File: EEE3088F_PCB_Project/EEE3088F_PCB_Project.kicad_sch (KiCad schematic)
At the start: 31 parts, among them IC1 DRV8833PWPR, IC2 DRV8833PWPR, IC3 TPS62067DSGR, IC4 TPS62067DSGR, IC5 INA219AIDCNR, J1 Conn_02x16_Odd_Even, Q3 MMBT2222A, Q4 MMBT2222A, Q5 AO3401A, Q6 AO3401A

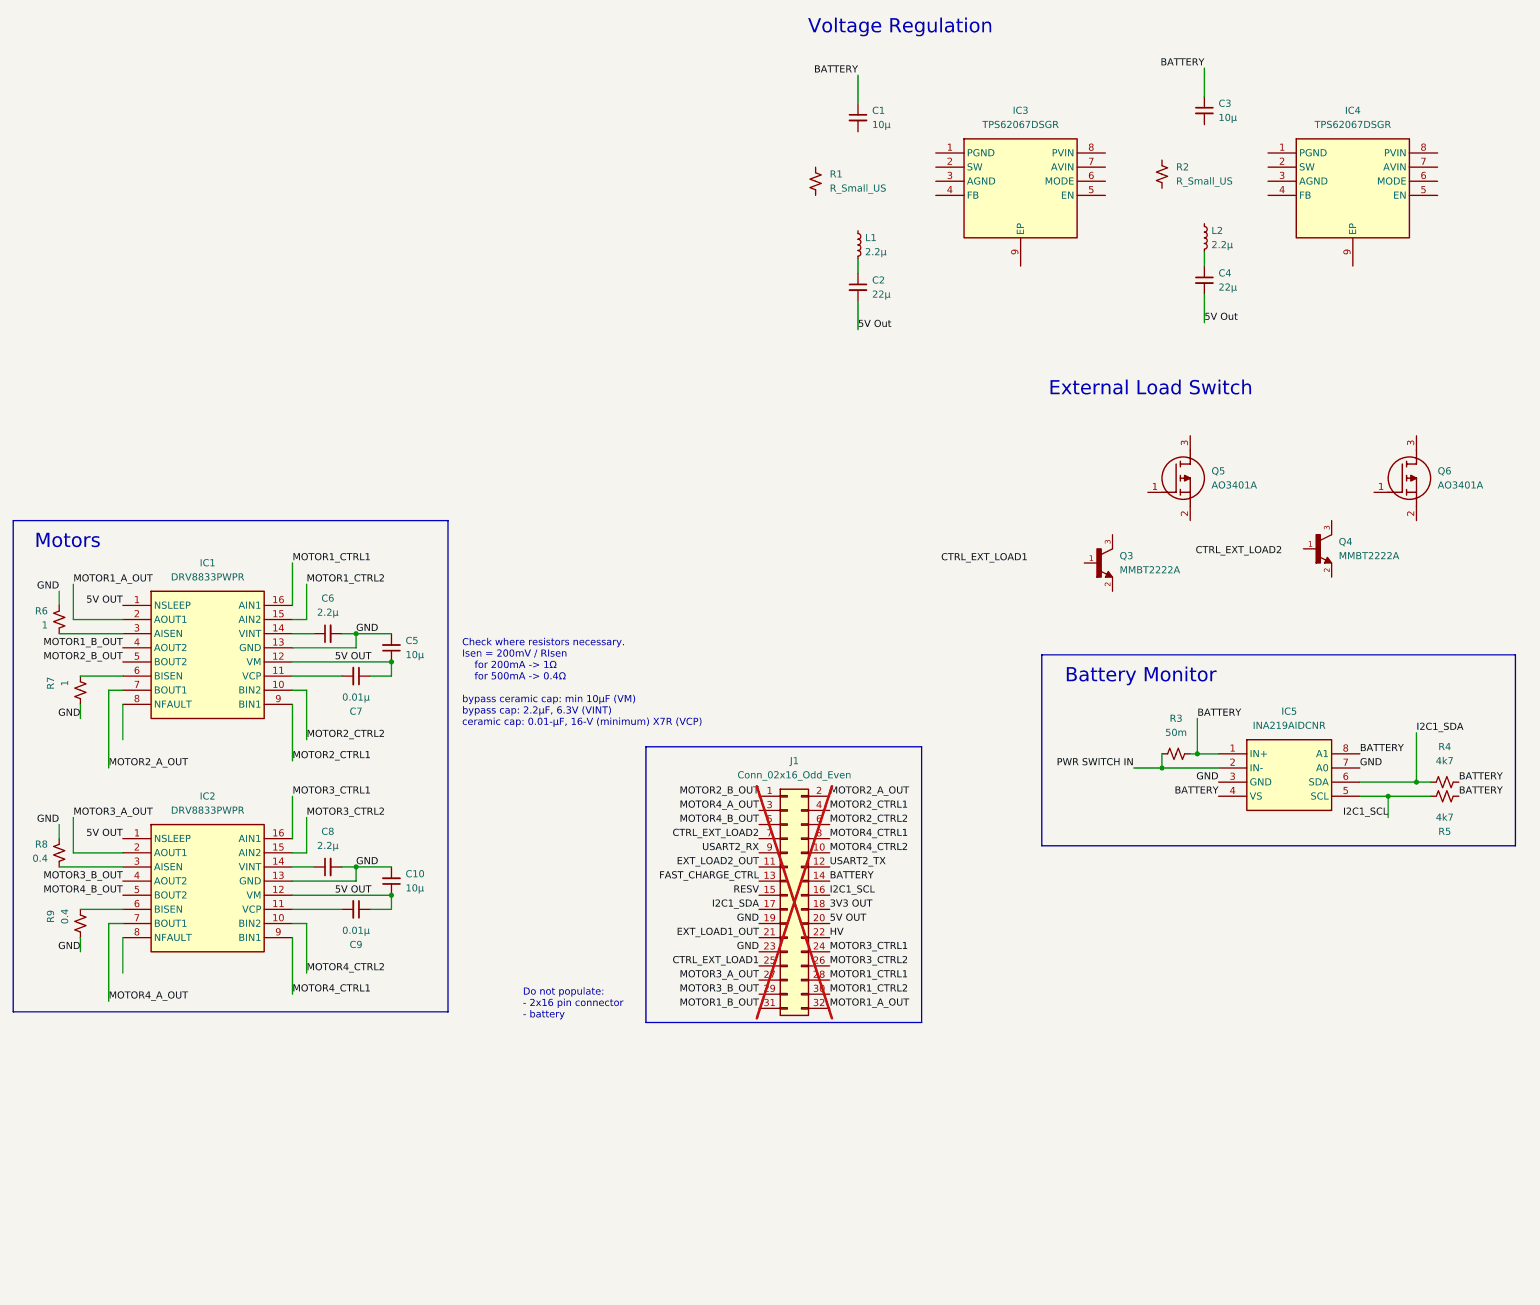
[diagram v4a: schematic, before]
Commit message: v0.4
Lula: rough voltage regulator circuits done but bias resistor values not calculated
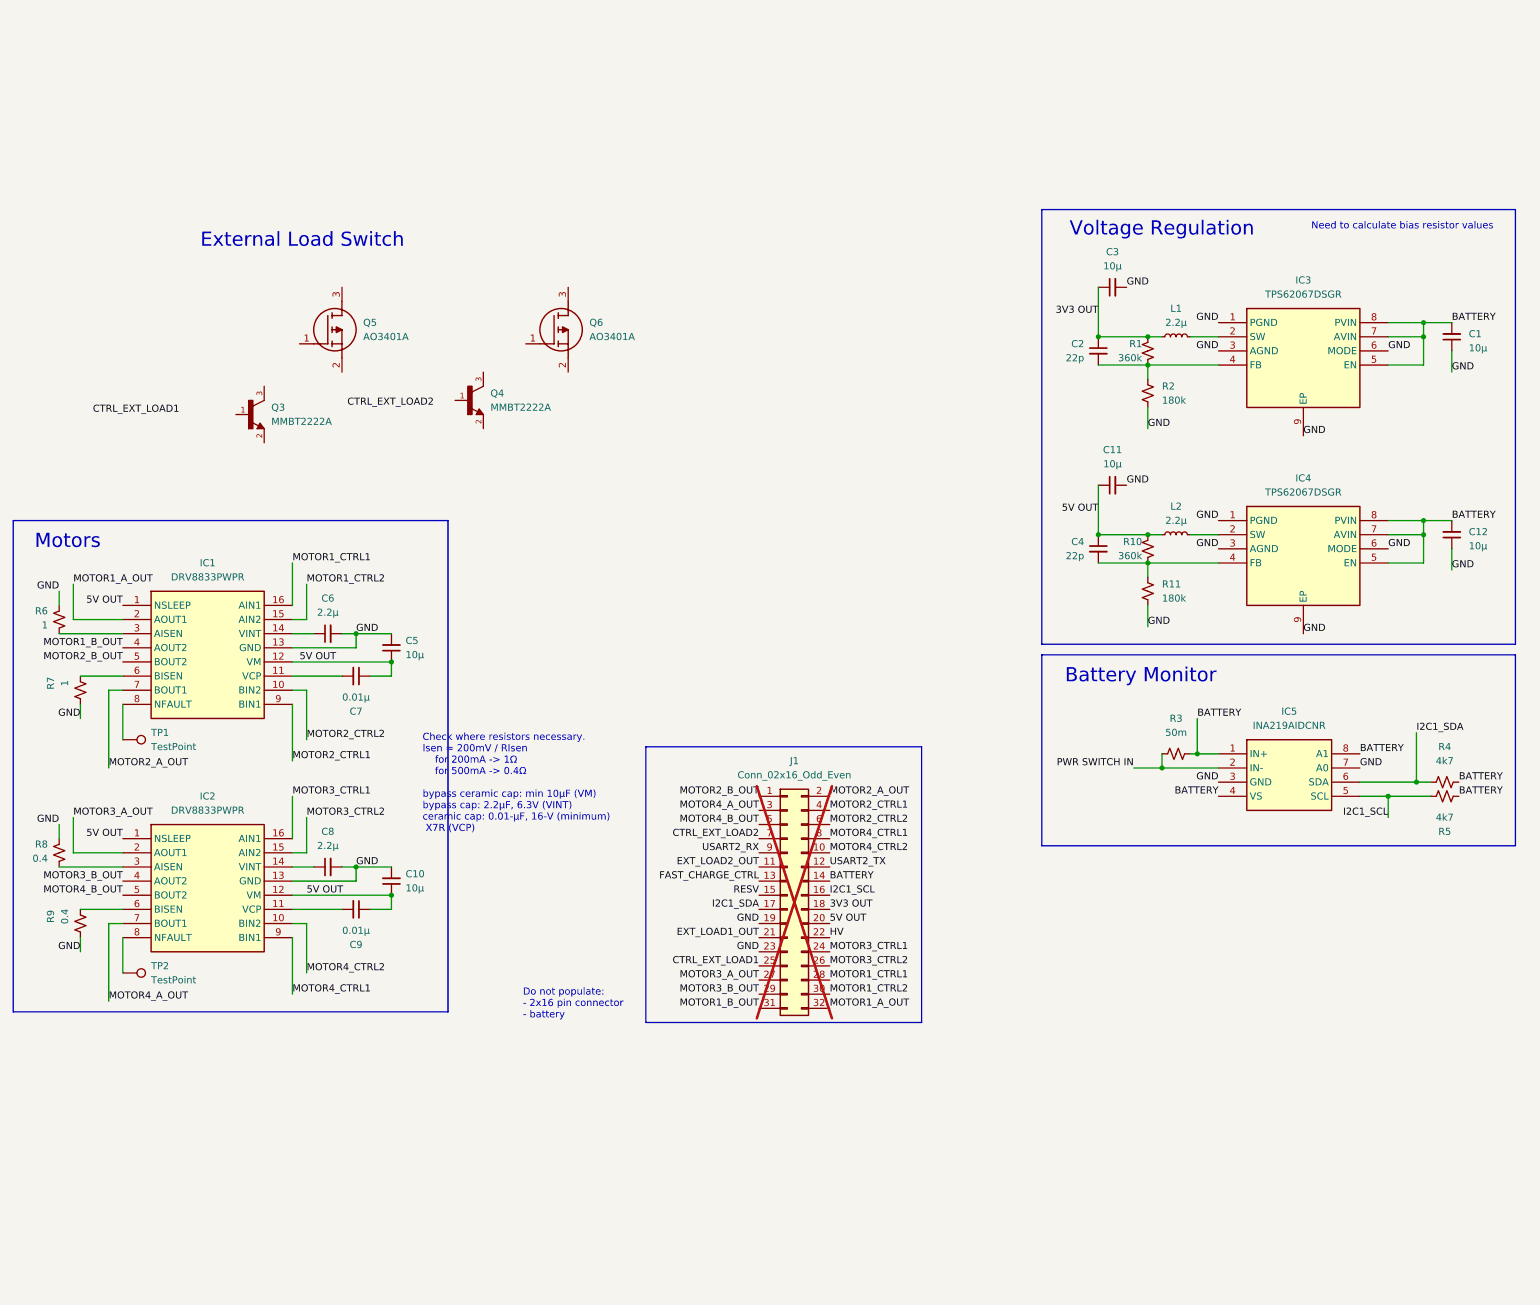
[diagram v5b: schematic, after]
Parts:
- added C11, C12: 10µ, symbol Device:C_Small
- added R10: 360k, symbol Device:R_Small_US
- added R11: 180k, symbol Device:R_Small_US
- added TP1, TP2: TestPoint, symbol Connector:TestPoint
- C2, C4: value 22µ -> 22p
- R1: value R_Small_US -> 360k
- R2: value R_Small_US -> 180k
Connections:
- net 3V3 OUT: now also C2.1, C3.1, L1.1, R1.1
- net 5V OUT: now also C4.1, L2.1, C11.1, R10.1
- net BATTERY: now also C1.2, IC3.5 (EN), IC3.7 (AVIN), IC3.8 (PVIN), IC4.5 (EN), IC4.7 (AVIN), IC4.8 (PVIN), C12.2; no longer C1.1, C3.1
- net GND: now also C1.1, C3.2, IC3.1 (PGND), IC3.3 (AGND), IC3.6 (MODE), IC3.9 (EP), IC4.1 (PGND), IC4.3 (AGND), IC4.6 (MODE), IC4.9 (EP), R2.2, C11.2, C12.1, R11.2
- net at IC3.2 (SW): now also L1.2
- net at IC3.4 (FB): now also C2.2, R1.2, R2.1
- net at IC2.8 (NFAULT): now also TP2.1
- net at L2.2: now also IC4.2 (SW); no longer C4.1
- net at IC1.8 (NFAULT): now also TP1.1
- net at IC4.4 (FB): now also C4.2, R10.2, R11.1
- removed net 5V Out: C2.2, C4.2
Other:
- note added: "Need to calculate bias resistor values"
- moved on the sheet: C1, L1, Q3, Q4, Q5, Q6

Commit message: v0.5
Lula: all my rough circuits done
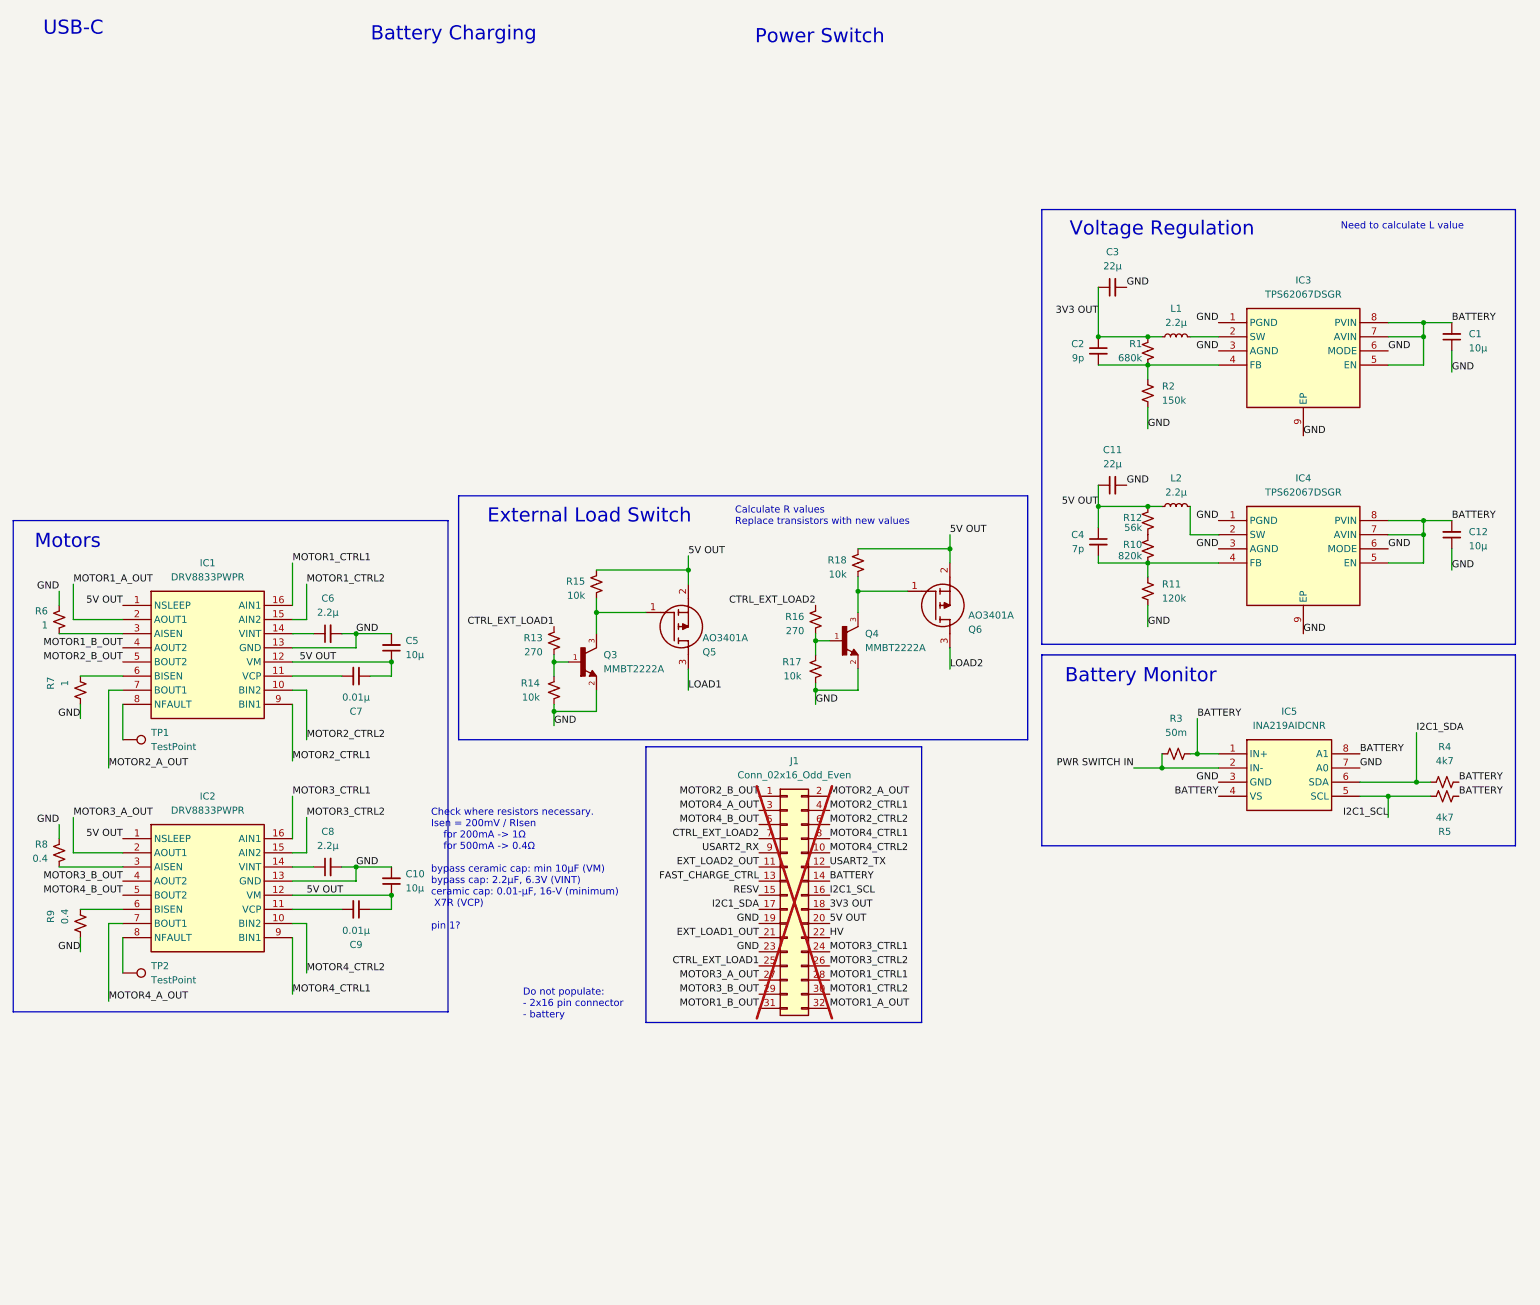
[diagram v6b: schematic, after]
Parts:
- added R12: 56k, symbol Device:R_Small_US
- added R13, R16: 270, symbol Device:R_Small_US
- added R14, R15, R17, R18: 10k, symbol Device:R_Small_US
- C11, C3: value 10µ -> 22µ
- C2: value 22p -> 9p
- C4: value 22p -> 7p
- R1: value 360k -> 680k
- R10: value 360k -> 820k
- R11: value 180k -> 120k
- R2: value 180k -> 150k
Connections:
- net 5V OUT: now also Q5.2 (S), Q6.2 (S), R12.1, R15.1, R18.1; no longer R10.1
- net CTRL_EXT_LOAD1: now also R13.1
- net CTRL_EXT_LOAD2: now also R16.1
- net GND: now also Q3.2, Q4.2, R14.2, R17.2
- net at Q5.1 (G): now also Q3.3, R15.2
- net LOAD1: now reaches Q5.3 (D)
- net at Q4.1: now also R16.2, R17.1
- net at Q4.3: now also Q6.1 (G), R18.2
- net at Q3.1: now also R13.2, R14.1
- net LOAD2: now reaches Q6.3 (D)
- new net: R10.1, R12.2
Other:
- note added: "Battery Charging"
- note added: "Calculate R values Replace transistors with new values"
- note added: "Check where resistors necessary. Isen = 200mV / RIsen for 200mA -> 1Ω for 500mA -> 0.4Ω bypass ceramic cap: min 10µF (VM) bypass cap: 2.2µF, 6.3V (VINT) ceramic cap: 0.01-μF, 16-V (minimum) X7R (VCP) pin 1?"
- note added: "Need to calculate L value"
- note added: "Power Switch"
- note added: "USB-C"
- note removed: "Check where resistors necessary. Isen = 200mV / RIsen for 200mA -> 1Ω for 500mA -> 0.4Ω bypass ceramic cap: min 10µF (VM) bypass cap: 2.2µF, 6.3V (VINT) ceramic cap: 0.01-μF, 16-V (minimum) X7R (VCP)"
- note removed: "Need to calculate bias resistor values"
- moved on the sheet: C4, L2, Q3, Q5

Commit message: v0.6
Lula:
- motors done
- some pcb footprints added
- imports updated
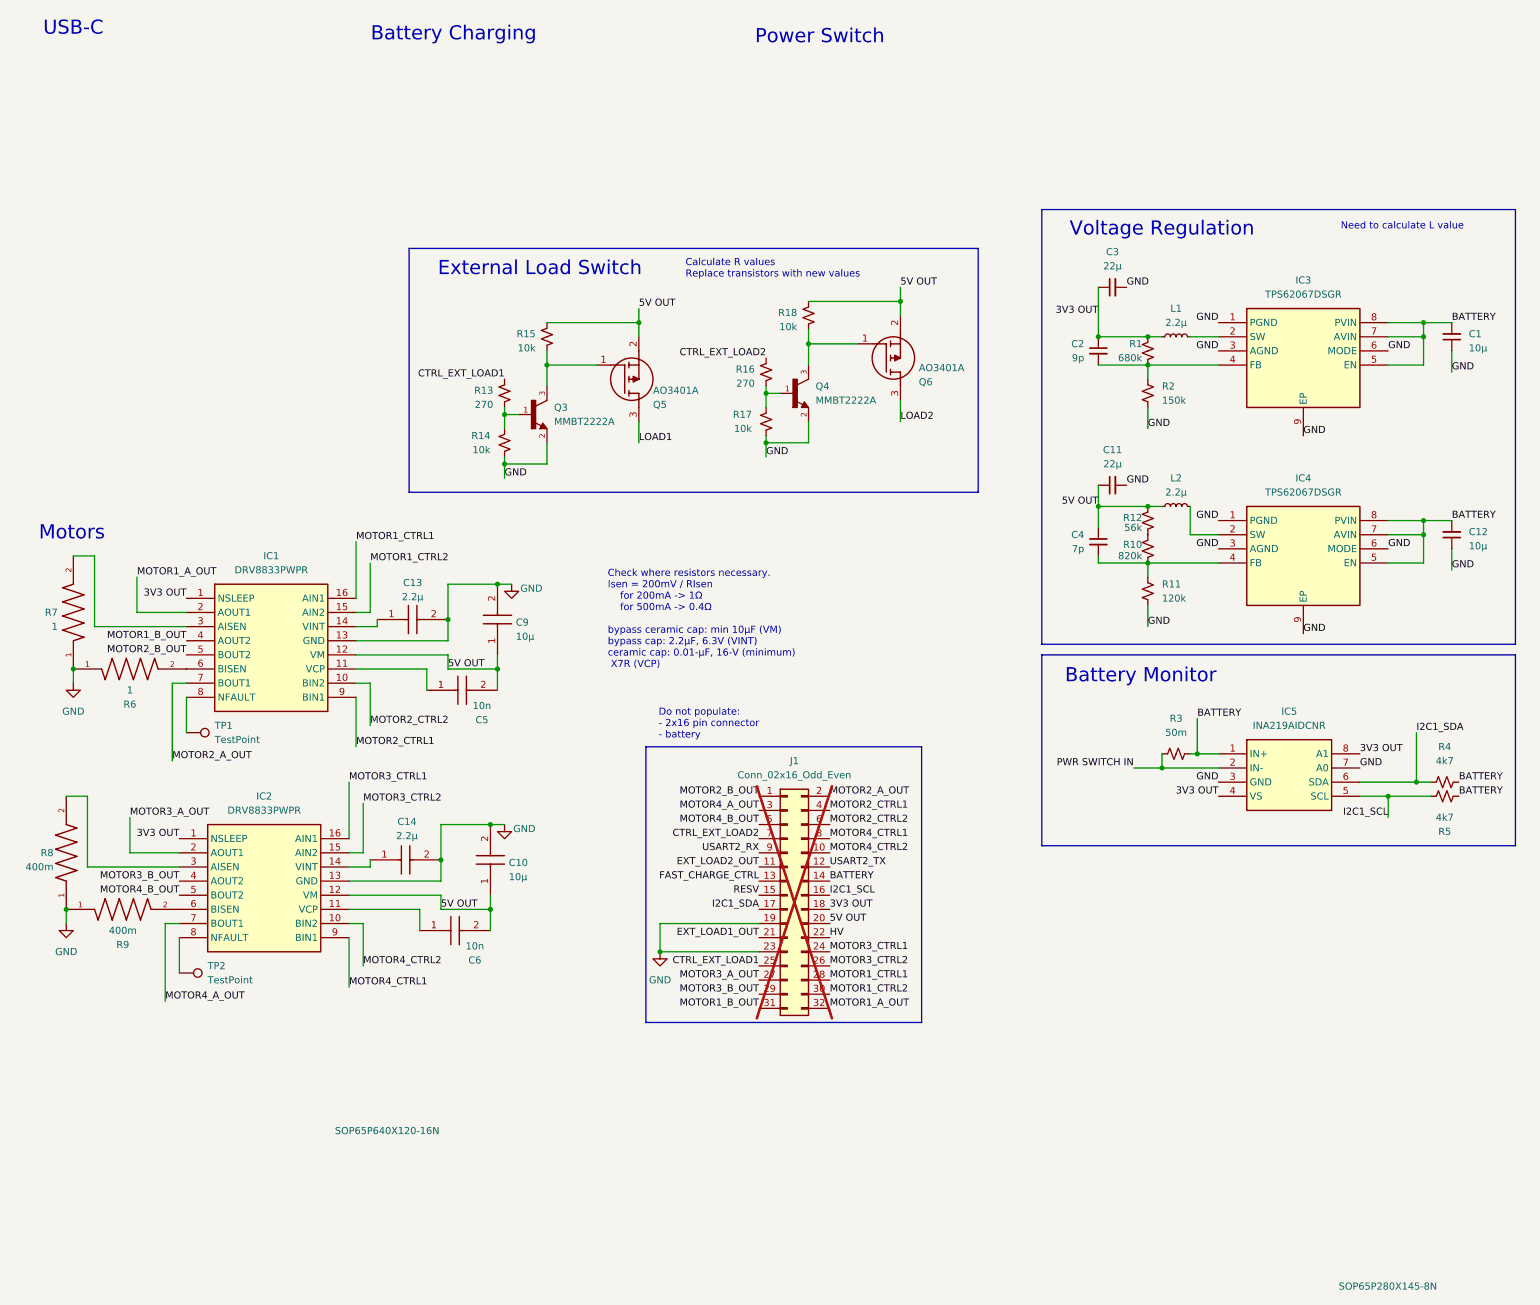
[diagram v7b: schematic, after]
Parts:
- removed C10, C5: 10µ, symbol Device:C_Small
- removed C6, C8: 2.2µ, symbol Device:C_Small
- removed C7, C9: 0.01µ, symbol Device:C_Small
- removed R6, R7: 1, symbol Device:R_Small_US
- removed R8, R9: 0.4, symbol Device:R_Small_US
- added C10, C9: 10µ, CAPC3216X180N, symbol CL31A106KBHNNNE:CL31A106KBHNNNE
- added C13, C14: 2.2µ, CAPC3216X180N, symbol CL31B225KBHNNNE:CL31B225KBHNNNE
- added C5, C6: 10n, CAPC2012X75N, symbol CL21B103KBANNNC:CL21B103KBANNNC
- added R6, R7: 1, 1206W4F100KT5E:RESC3115X65N, symbol 1206W4F100KT5E:1206W4F100KT5E
- added R8, R9: 400m, 1206W4F400LT5E:RESC3115X65N, symbol 1206W4F400LT5E:1206W4F400LT5E
- J1: footprint (none) -> Connector_Samtec_HLE_THT:Samtec_HLE-116-02-xx-DV-TE_2x16_P2.54mm_Horizontal
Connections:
- net 3V3 OUT: now also IC1.1 (NSLEEP), IC2.1 (NSLEEP), IC5.4 (VS), IC5.8 (A1)
- net 5V OUT: now also C10.1, C5.2, C6.2, C9.1; no longer IC1.1 (NSLEEP), IC2.1 (NSLEEP)
- net BATTERY: no longer IC5.4 (VS), IC5.8 (A1)
- net GND: now also C10.2, C13.2, C14.2, C9.2, R6.1, R7.1, R8.1, R9.1
- net at IC2.14 (VINT): now also C14.1
- net at IC1.14 (VINT): now also C13.1
- net at IC1.3 (AISEN): now also R7.2
- net at IC2.11 (VCP): now also C6.1
- net at IC2.3 (AISEN): now also R8.2
- net at IC2.6 (BISEN): now also R9.2
- net at IC1.11 (VCP): now also C5.1
- net at IC1.6 (BISEN): now also R6.2
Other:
- note added: "Check where resistors necessary. Isen = 200mV / RIsen for 200mA -> 1Ω for 500mA -> 0.4Ω bypass ceramic cap: min 10µF (VM) bypass cap: 2.2µF, 6.3V (VINT) ceramic cap: 0.01-μF, 16-V (minimum) X7R (VCP)"
- note removed: "Check where resistors necessary. Isen = 200mV / RIsen for 200mA -> 1Ω for 500mA -> 0.4Ω bypass ceramic cap: min 10µF (VM) bypass cap: 2.2µF, 6.3V (VINT) ceramic cap: 0.01-μF, 16-V (minimum) X7R (VCP) pin 1?"
- moved on the sheet: IC1, IC2, Q3, Q4, Q5, Q6, R13, R14, R15, R16, R17, R18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
